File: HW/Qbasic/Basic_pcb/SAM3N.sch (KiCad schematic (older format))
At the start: 33 parts, among them P1 CONN_02X02, U11 ZLDO1117G33TA, X401 12MHz

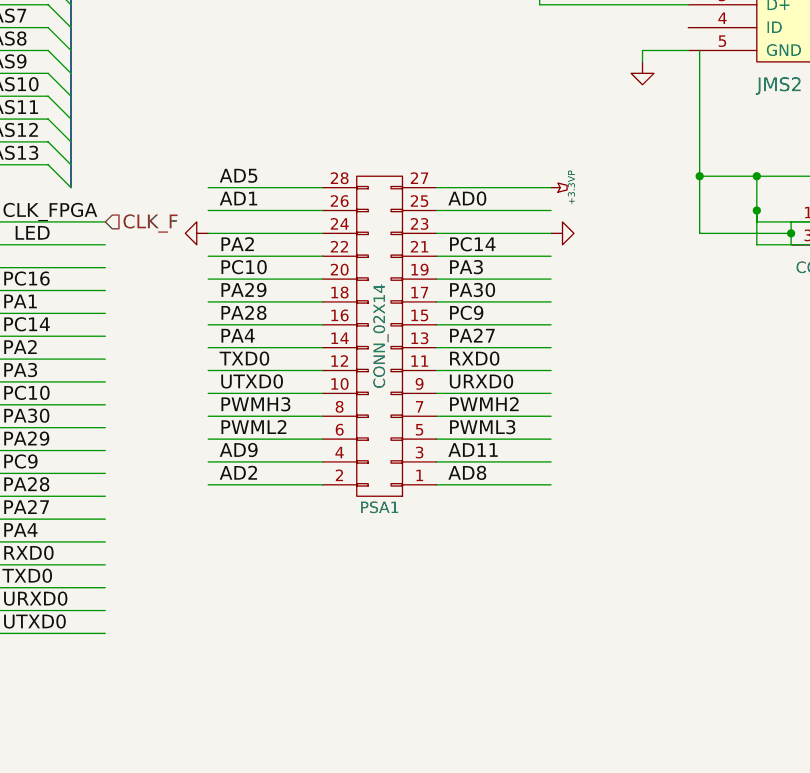
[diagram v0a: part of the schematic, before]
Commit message: schematic connections checked and finished
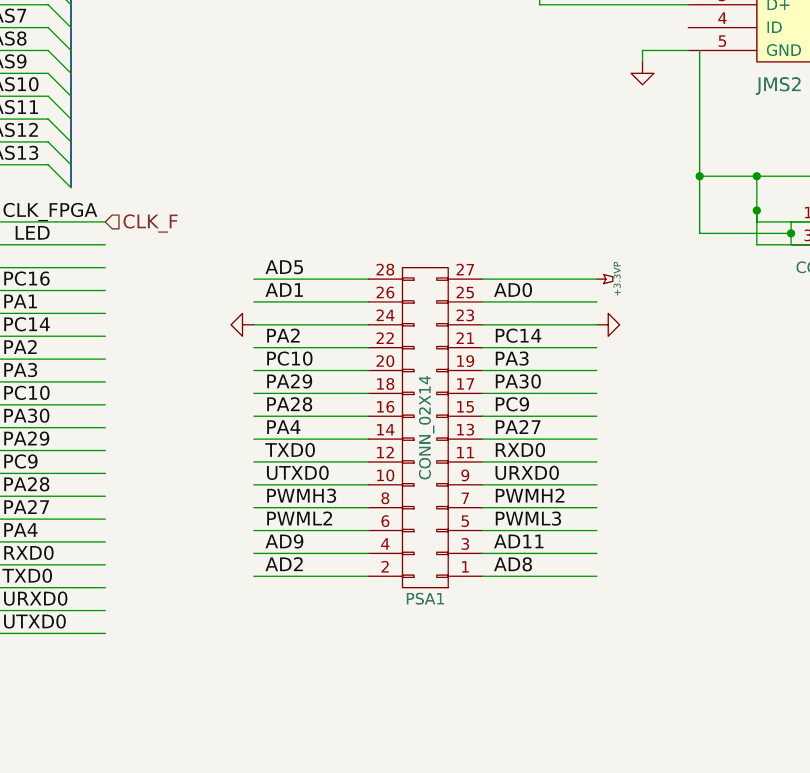
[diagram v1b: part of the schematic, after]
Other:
- moved on the sheet: PSA1
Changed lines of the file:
@@
 L CONN_02X14 PSA1
 U 1 1 54C40123
-P 6600 5100
-F 0 "PSA1" H 6600 5850 50  0000 C CNN
-F 1 "CONN_02X14" V 6600 5100 50  0000 C CNN
-F 2 "Socket_Strips:Socket_Strip_Straight_2x14" H 6600 3950 60  0001 C CNN
-F 3 "" H 6600 3950 60  0000 C CNN
-	1    6600 5100
+P 6800 5500
+F 0 "PSA1" H 6800 6250 50  0000 C CNN
+F 1 "CONN_02X14" V 6800 5500 50  0000 C CNN
+F 2 "Socket_Strips:Socket_Strip_Straight_2x14" H 6800 4350 60  0001 C CNN
+F 3 "" H 6800 4350 60  0000 C CNN
+	1    6800 5500
 	-1   0    0    1
 $EndComp
@@
 Text Label 1150 5700 0    60   ~ 0
 AD3
-Text Label 5900 4450 0    60   ~ 0
+Text Label 6100 4850 0    60   ~ 0
 AD5
-Text Label 6900 4550 0    60   ~ 0
+Text Label 7100 4950 0    60   ~ 0
 AD0
-Text Label 5900 4550 0    60   ~ 0
+Text Label 6100 4950 0    60   ~ 0
 AD1
-Text Label 6900 5650 0    60   ~ 0
+Text Label 7100 6050 0    60   ~ 0
 AD11
-Text Label 5900 5750 0    60   ~ 0
+Text Label 6100 6150 0    60   ~ 0
 AD2
-Text Label 6900 5750 0    60   ~ 0
+Text Label 7100 6150 0    60   ~ 0
 AD8
-Text Label 5900 5650 0    60   ~ 0
+Text Label 6100 6050 0    60   ~ 0
 AD9
 Text Label 1150 5800 0    60   ~ 0
@@
 Text Label 1150 6600 0    60   ~ 0
 PWMH0
-Text Label 5900 5550 0    60   ~ 0
+Text Label 6100 5950 0    60   ~ 0
 PWML2
-Text Label 6900 5550 0    60   ~ 0
+Text Label 7100 5950 0    60   ~ 0
 PWML3
-Text Label 5900 5450 0    60   ~ 0
+Text Label 6100 5850 0    60   ~ 0
 PWMH3
-Text Label 6900 5450 0    60   ~ 0
+Text Label 7100 5850 0    60   ~ 0
 PWMH2
 Text Label 4950 6300 0    60   ~ 0
@@
 Text Label 4950 6200 0    60   ~ 0
 TXD0
-Text Label 6900 5350 0    60   ~ 0
+Text Label 7100 5750 0    60   ~ 0
 URXD0
-Text Label 5900 5350 0    60   ~ 0
+Text Label 6100 5750 0    60   ~ 0
 UTXD0
-Text Label 5900 5250 0    60   ~ 0
+Text Label 6100 5650 0    60   ~ 0
 TXD0
-Text Label 6900 5250 0    60   ~ 0
+Text Label 7100 5650 0    60   ~ 0
 RXD0
 Text Label 4950 6000 0    60   ~ 0
@@
 Text Label 4950 4900 0    60   ~ 0
 PC16
-Text Label 5900 5150 0    60   ~ 0
+Text Label 6100 5550 0    60   ~ 0
 PA4
-Text Label 6900 5150 0    60   ~ 0
+Text Label 7100 5550 0    60   ~ 0
 PA27
-Text Label 5900 5050 0    60   ~ 0
+Text Label 6100 5450 0    60   ~ 0
 PA28
-Text Label 6900 5050 0    60   ~ 0
+Text Label 7100 5450 0    60   ~ 0
 PC9
-Text Label 5900 4950 0    60   ~ 0
+Text Label 6100 5350 0    60   ~ 0
 PA29
-Text Label 6900 4950 0    60   ~ 0
+Text Label 7100 5350 0    60   ~ 0
 PA30
-Text Label 5900 4850 0    60   ~ 0
+Text Label 6100 5250 0    60   ~ 0
 PC10
-Text Label 6900 4850 0    60   ~ 0
+Text Label 7100 5250 0    60   ~ 0
 PA3
-Text Label 5900 4750 0    60   ~ 0
+Text Label 6100 5150 0    60   ~ 0
 PA2
-Text Label 6900 4750 0    60   ~ 0
+Text Label 7100 5150 0    60   ~ 0
 PC14
 Text Label 5000 4700 0    60   ~ 0
@@
 L +3.3VP #PWR024
 U 1 1 54ED0F5F
-P 7350 4450
-F 0 "#PWR024" H 7400 4480 20  0001 C CNN
-F 1 "+3.3VP" H 7350 4540 30  0000 C CNN
-F 2 "" H 7350 4450 60  0001 C CNN
-F 3 "" H 7350 4450 60  0001 C CNN
-	1    7350 4450
+P 7550 4850
+F 0 "#PWR024" H 7600 4880 20  0001 C CNN
+F 1 "+3.3VP" H 7550 4940 30  0000 C CNN
+F 2 "" H 7550 4850 60  0001 C CNN
+F 3 "" H 7550 4850 60  0001 C CNN
+	1    7550 4850
 	0    1    1    0
 $EndComp
@@
 L GND #PWR025
 U 1 1 54ED12AC
-P 7350 4650
-F 0 "#PWR025" H 7350 4650 30  0001 C CNN
-F 1 "GND" H 7350 4580 30  0001 C CNN
-F 2 "" H 7350 4650 60  0001 C CNN
-F 3 "" H 7350 4650 60  0001 C CNN
-	1    7350 4650
+P 7550 5050
+F 0 "#PWR025" H 7550 5050 30  0001 C CNN
+F 1 "GND" H 7550 4980 30  0001 C CNN
+F 2 "" H 7550 5050 60  0001 C CNN
+F 3 "" H 7550 5050 60  0001 C CNN
+	1    7550 5050
 	0    -1   -1   0
 $EndComp
@@
 L GND #PWR029
 U 1 1 555D26A9
-P 5850 4650
-F 0 "#PWR029" H 5850 4650 30  0001 C CNN
-F 1 "GND" H 5850 4580 30  0001 C CNN
-F 2 "" H 5850 4650 60  0001 C CNN
-F 3 "" H 5850 4650 60  0001 C CNN
-	1    5850 4650
+P 6050 5050
+F 0 "#PWR029" H 6050 5050 30  0001 C CNN
+F 1 "GND" H 6050 4980 30  0001 C CNN
+F 2 "" H 6050 5050 60  0001 C CNN
+F 3 "" H 6050 5050 60  0001 C CNN
+	1    6050 5050
 	0    1    1    0
 $EndComp
@@
 	1100 5700 1600 5700
 Wire Wire Line
-	5850 4450 6350 4450
-Wire Wire Line
-	6850 4550 7350 4550
-Wire Wire Line
-	5850 4550 6350 4550
-Wire Wire Line
-	6850 5650 7350 5650
-Wire Wire Line
-	5850 5750 6350 5750
-Wire Wire Line
-	6850 5750 7350 5750
-Wire Wire Line
-	5850 5650 6350 5650
+	6050 4850 6550 4850
+Wire Wire Line
+	7050 4950 7550 4950
+Wire Wire Line
+	6050 4950 6550 4950
+Wire Wire Line
+	7050 6050 7550 6050
+Wire Wire Line
+	6050 6150 6550 6150
+Wire Wire Line
+	7050 6150 7550 6150
+Wire Wire Line
+	6050 6050 6550 6050
 Wire Wire Line
 	1100 5800 1600 5800
@@
 	1100 6600 1600 6600
 Wire Wire Line
-	6850 5550 7350 5550
-Wire Wire Line
-	5850 5550 6350 5550
-Wire Wire Line
-	6850 5450 7350 5450
-Wire Wire Line
-	5850 5450 6350 5450
+	7050 5950 7550 5950
+Wire Wire Line
+	6050 5950 6550 5950
+Wire Wire Line
+	7050 5850 7550 5850
+Wire Wire Line
+	6050 5850 6550 5850
 Wire Wire Line
 	4900 6300 5400 6300
@@
 	4900 6200 5400 6200
 Wire Wire Line
-	6850 5350 7350 5350
-Wire Wire Line
-	5850 5350 6350 5350
-Wire Wire Line
-	5850 5250 6350 5250
-Wire Wire Line
-	6850 5250 7350 5250
+	7050 5750 7550 5750
+Wire Wire Line
+	6050 5750 6550 5750
+Wire Wire Line
+	6050 5650 6550 5650
+Wire Wire Line
+	7050 5650 7550 5650
 Wire Wire Line
 	5400 6000 4900 6000
@@
 	5400 4600 4900 4600
 Wire Wire Line
-	6350 5150 5850 5150
-Wire Wire Line
-	7350 5150 6850 5150
-Wire Wire Line
-	6350 5050 5850 5050
-Wire Wire Line
-	7350 5050 6850 5050
-Wire Wire Line
-	6350 4950 5850 4950
-Wire Wire Line
-	7350 4950 6850 4950
-Wire Wire Line
-	6350 4850 5850 4850
-Wire Wire Line
-	7350 4850 6850 4850
-Wire Wire Line
-	6350 4750 5850 4750
-Wire Wire Line
-	7350 4750 6850 4750
-Wire Wire Line
-	6350 4650 5850 4650
-Wire Wire Line
-	6850 4650 7350 4650
+	6550 5550 6050 5550
+Wire Wire Line
+	7550 5550 7050 5550
+Wire Wire Line
+	6550 5450 6050 5450
+Wire Wire Line
+	7550 5450 7050 5450
+Wire Wire Line
+	6550 5350 6050 5350
+Wire Wire Line
+	7550 5350 7050 5350
+Wire Wire Line
+	6550 5250 6050 5250
+Wire Wire Line
+	7550 5250 7050 5250
+Wire Wire Line
+	6550 5150 6050 5150
+Wire Wire Line
+	7550 5150 7050 5150
+Wire Wire Line
+	6550 5050 6050 5050
+Wire Wire Line
+	7050 5050 7550 5050
 Wire Wire Line
 	7400 3550 7950 3550
@@
 Connection ~ 8250 4550
 Wire Wire Line
-	6850 4450 7350 4450
+	7050 4850 7550 4850
 $EndSCHEMATC

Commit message: version final antes de  planos de tierra
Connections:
- wire segments 227 -> 229
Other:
- note added: "se cambia en la tarjeta original el pa19 por el pa23"
- note added: "se puente el pa23 a pa19"
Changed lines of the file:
@@
 	1100 5300 1600 5300
 Wire Wire Line
-	1100 5400 1600 5400
+	850  5400 1600 5400
 Wire Wire Line
 	1100 5500 1600 5500
@@
 Wire Wire Line
 	7050 4850 7550 4850
+Wire Wire Line
+	1600 5600 850  5600
+Wire Wire Line
+	850  5600 850  5400
+Text Notes 500  5600 0    60   ~ 0
+se puente el pa23 a pa19
+Text Notes 6000 6350 0    60   ~ 0
+se cambia en la tarjeta original el pa19 por el pa23
 $EndSCHEMATC
